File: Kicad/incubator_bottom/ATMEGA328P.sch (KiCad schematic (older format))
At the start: 5 parts, among them U3 ATmega328P-AU

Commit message: updated: first push in Lau
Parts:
- C1, C2: symbol Device:C -> incubator_bottom-rescue:C-Device
- JP1: symbol Jumper:SolderJumper_2_Open -> incubator_bottom-rescue:SolderJumper_2_Open-Jumper
- R12: symbol Device:R -> incubator_bottom-rescue:R-Device
- U3: symbol MCU_Microchip_ATmega:ATmega328P-AU -> incubator_bottom-rescue:ATmega328P-AU-MCU_Microchip_ATmega
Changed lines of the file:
@@
 $EndDescr
 $Comp
-L MCU_Microchip_ATmega:ATmega328P-AU U3
+L incubator_bottom-rescue:ATmega328P-AU-MCU_Microchip_ATmega U3
 U 1 1 610AABC9
 P 6175 3625
@@
 $EndComp
 $Comp
-L power:VCC #PWR0119
+L incubator_bottom-rescue:VCC-power #PWR0119
 U 1 1 610AABCF
 P 6175 1950
@@
 $EndComp
 $Comp
-L Device:C C2
+L incubator_bottom-rescue:C-Device C2
 U 1 1 610AABD5
 P 4925 2275
@@
 $EndComp
 $Comp
-L Device:C C1
+L incubator_bottom-rescue:C-Device C1
 U 1 1 610AABDB
 P 4600 2275
@@
 Connection ~ 4925 2050
 $Comp
-L power:GND #PWR0120
+L incubator_bottom-rescue:GND-power #PWR0120
 U 1 1 610AABE5
 P 4600 2525
@@
 Connection ~ 4600 2475
 $Comp
-L power:VCC #PWR0121
+L incubator_bottom-rescue:VCC-power #PWR0121
 U 1 1 610AABF0
 P 5150 3400
@@
 ~RESET
 $Comp
-L Device:R R12
+L incubator_bottom-rescue:R-Device R12
 U 1 1 610AAC20
 P 5150 3675
@@
 D7
 $Comp
-L power:GND #PWR0122
+L incubator_bottom-rescue:GND-power #PWR0122
 U 1 1 610AAC01
 P 5150 4350
@@
 GND
 $Comp
-L power:GND #PWR0123
+L incubator_bottom-rescue:GND-power #PWR0123
 U 1 1 610AAC08
 P 6175 5250
@@
 	6275 2050 6175 2050
 $Comp
-L Jumper:SolderJumper_2_Open JP1
+L incubator_bottom-rescue:SolderJumper_2_Open-Jumper JP1
 U 1 1 61118ECF
 P 5150 4125

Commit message: feat: v1.0.1 of board
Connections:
- net ERROR: now reaches U3.14 (PB2)
- no-connect marks 8 -> 7
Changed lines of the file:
@@
 NoConn ~ 6775 2425
 NoConn ~ 6775 2525
-NoConn ~ 6775 2625
 NoConn ~ 6775 3025
 NoConn ~ 6775 3125
@@
 	0    1    1    0
 $EndComp
+Text HLabel 6850 2625 2    50   Input ~ 0
+ERROR
+Wire Wire Line
+	6775 2625 6850 2625
 $EndSCHEMATC

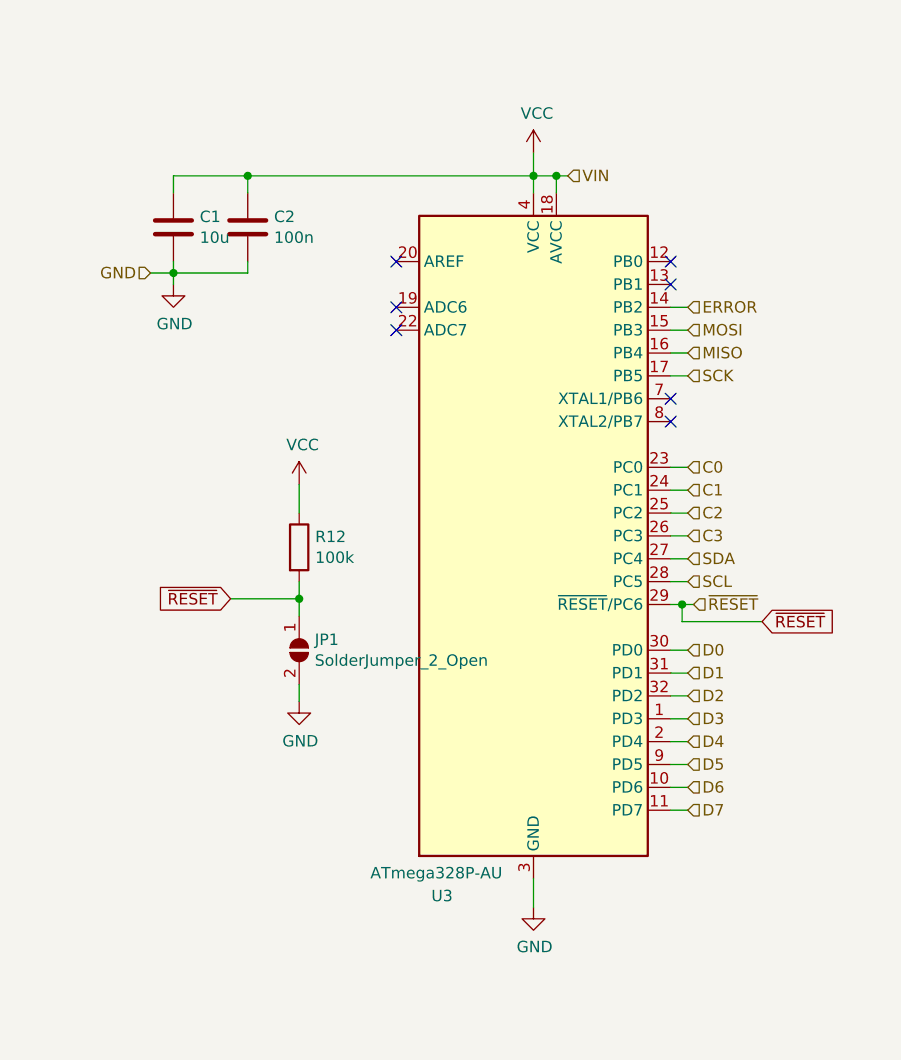
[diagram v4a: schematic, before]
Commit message: fix: version 1.0.2 of the PCB change size holes M4 -> M3 and changes their position
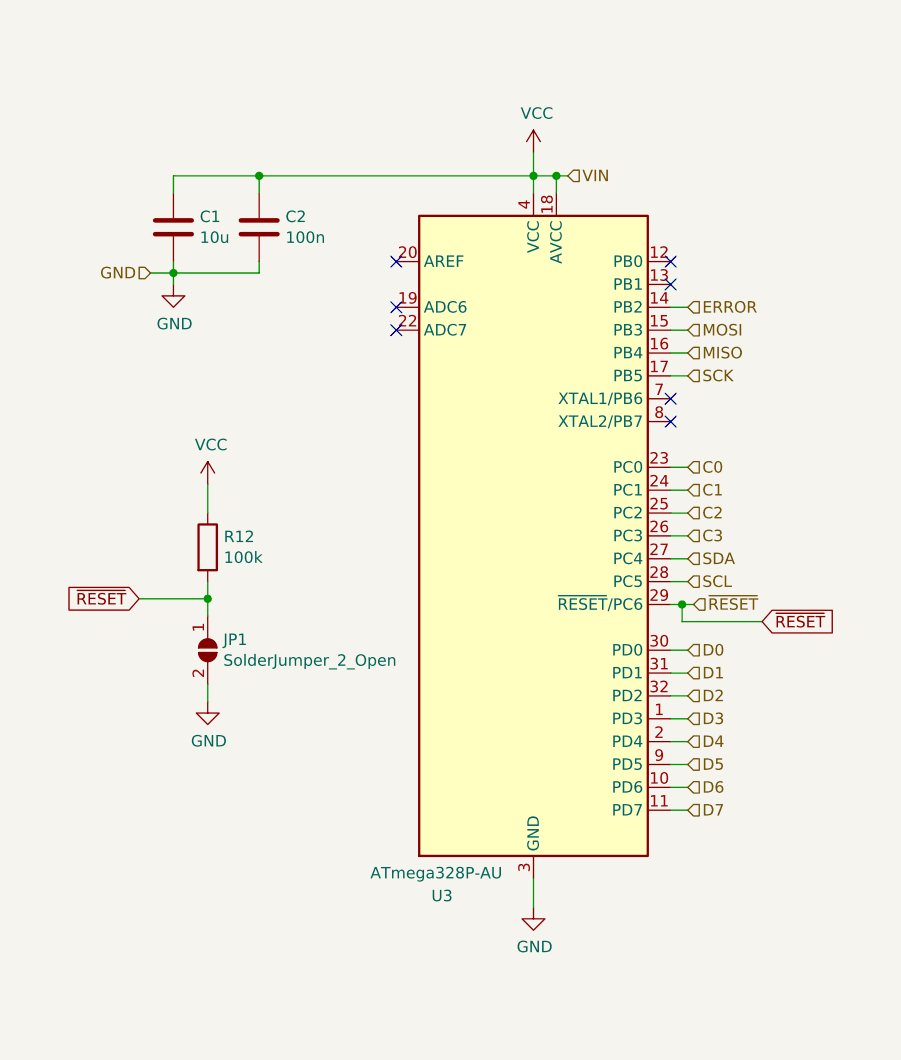
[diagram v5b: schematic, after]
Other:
- moved on the sheet: C2, JP1, R12
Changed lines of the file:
@@
 L incubator_bottom-rescue:C-Device C2
 U 1 1 610AABD5
-P 4925 2275
-F 0 "C2" H 5040 2321 50  0000 L CNN
-F 1 "100n" H 5040 2230 50  0000 L CNN
-F 2 "Capacitor_SMD:C_0805_2012Metric_Pad1.18x1.45mm_HandSolder" H 4963 2125 50  0001 C CNN
-F 3 "~" H 4925 2275 50  0001 C CNN
-	1    4925 2275
+P 4975 2275
+F 0 "C2" H 5090 2321 50  0000 L CNN
+F 1 "100n" H 5090 2230 50  0000 L CNN
+F 2 "Capacitor_SMD:C_0805_2012Metric_Pad1.18x1.45mm_HandSolder" H 5013 2125 50  0001 C CNN
+F 3 "~" H 4975 2275 50  0001 C CNN
+	1    4975 2275
 	1    0    0    -1
 $EndComp
@@
 $EndComp
 Wire Wire Line
-	4925 2125 4925 2050
-Wire Wire Line
 	4600 2125 4600 2050
-Wire Wire Line
-	4600 2050 4925 2050
-Connection ~ 4925 2050
 $Comp
 L incubator_bottom-rescue:GND-power #PWR0120
@@
 $EndComp
 Wire Wire Line
-	4925 2425 4925 2475
-Wire Wire Line
-	4925 2475 4600 2475
-Wire Wire Line
 	4600 2475 4600 2425
 Wire Wire Line
@@
 L incubator_bottom-rescue:VCC-power #PWR0121
 U 1 1 610AABF0
-P 5150 3400
-F 0 "#PWR0121" H 5150 3250 50  0001 C CNN
-F 1 "VCC" H 5165 3573 50  0000 C CNN
-F 2 "" H 5150 3400 50  0001 C CNN
-F 3 "" H 5150 3400 50  0001 C CNN
-	1    5150 3400
-	1    0    0    -1
-$EndComp
-Wire Wire Line
-	5150 3400 5150 3525
-Wire Wire Line
-	4850 3900 5150 3900
-Wire Wire Line
-	5150 3900 5150 3825
-Wire Wire Line
-	5150 3975 5150 3900
-Connection ~ 5150 3900
-Wire Wire Line
-	5150 4350 5150 4275
-Wire Wire Line
-	4925 2050 6175 2050
+P 4750 3400
+F 0 "#PWR0121" H 4750 3250 50  0001 C CNN
+F 1 "VCC" H 4765 3573 50  0000 C CNN
+F 2 "" H 4750 3400 50  0001 C CNN
+F 3 "" H 4750 3400 50  0001 C CNN
+	1    4750 3400
+	1    0    0    -1
+$EndComp
+Wire Wire Line
+	4750 3400 4750 3525
+Wire Wire Line
+	4450 3900 4750 3900
+Wire Wire Line
+	4750 3900 4750 3825
+Wire Wire Line
+	4750 3975 4750 3900
+Connection ~ 4750 3900
+Wire Wire Line
+	4750 4350 4750 4275
 Connection ~ 6175 2050
 Wire Wire Line
@@
 Wire Wire Line
 	6850 2725 6775 2725
-Text GLabel 4850 3900 0    50   Input ~ 0
+Text GLabel 4450 3900 0    50   Input ~ 0
 ~RESET
 $Comp
 L incubator_bottom-rescue:R-Device R12
 U 1 1 610AAC20
-P 5150 3675
-F 0 "R12" H 5220 3721 50  0000 L CNN
-F 1 "100k" H 5220 3630 50  0000 L CNN
-F 2 "Resistor_SMD:R_0805_2012Metric_Pad1.20x1.40mm_HandSolder" V 5080 3675 50  0001 C CNN
-F 3 "~" H 5150 3675 50  0001 C CNN
-	1    5150 3675
+P 4750 3675
+F 0 "R12" H 4820 3721 50  0000 L CNN
+F 1 "100k" H 4820 3630 50  0000 L CNN
+F 2 "Resistor_SMD:R_0805_2012Metric_Pad1.20x1.40mm_HandSolder" V 4680 3675 50  0001 C CNN
+F 3 "~" H 4750 3675 50  0001 C CNN
+	1    4750 3675
 	1    0    0    -1
 $EndComp
@@
 L incubator_bottom-rescue:GND-power #PWR0122
 U 1 1 610AAC01
-P 5150 4350
-F 0 "#PWR0122" H 5150 4100 50  0001 C CNN
-F 1 "GND" H 5155 4177 50  0000 C CNN
-F 2 "" H 5150 4350 50  0001 C CNN
-F 3 "" H 5150 4350 50  0001 C CNN
-	1    5150 4350
+P 4750 4350
+F 0 "#PWR0122" H 4750 4100 50  0001 C CNN
+F 1 "GND" H 4755 4177 50  0000 C CNN
+F 2 "" H 4750 4350 50  0001 C CNN
+F 3 "" H 4750 4350 50  0001 C CNN
+	1    4750 4350
 	1    0    0    -1
 $EndComp
@@
 L incubator_bottom-rescue:SolderJumper_2_Open-Jumper JP1
 U 1 1 61118ECF
-P 5150 4125
-F 0 "JP1" V 5104 4193 50  0000 L CNN
-F 1 "SolderJumper_2_Open" V 5195 4193 50  0000 L CNN
-F 2 "Jumper:SolderJumper-2_P1.3mm_Open_RoundedPad1.0x1.5mm" H 5150 4125 50  0001 C CNN
-F 3 "~" H 5150 4125 50  0001 C CNN
-	1    5150 4125
+P 4750 4125
+F 0 "JP1" V 4704 4193 50  0000 L CNN
+F 1 "SolderJumper_2_Open" V 4795 4193 50  0000 L CNN
+F 2 "Jumper:SolderJumper-2_P1.3mm_Open_RoundedPad1.0x1.5mm" H 4750 4125 50  0001 C CNN
+F 3 "~" H 4750 4125 50  0001 C CNN
+	1    4750 4125
 	0    1    1    0
 $EndComp
@@
 Wire Wire Line
 	6775 2625 6850 2625
+Wire Wire Line
+	4975 2475 4975 2425
+Wire Wire Line
+	4600 2475 4975 2475
+Wire Wire Line
+	4600 2050 4975 2050
+Wire Wire Line
+	4975 2125 4975 2050
+Connection ~ 4975 2050
+Wire Wire Line
+	4975 2050 6175 2050
 $EndSCHEMATC
